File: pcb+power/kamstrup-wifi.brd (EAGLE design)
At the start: 36 x 81.3 mm, 26 parts, among them T1 BT137, T2 BT137, U1 ESP8266-07, U2 MCP1316T-29LE/OT

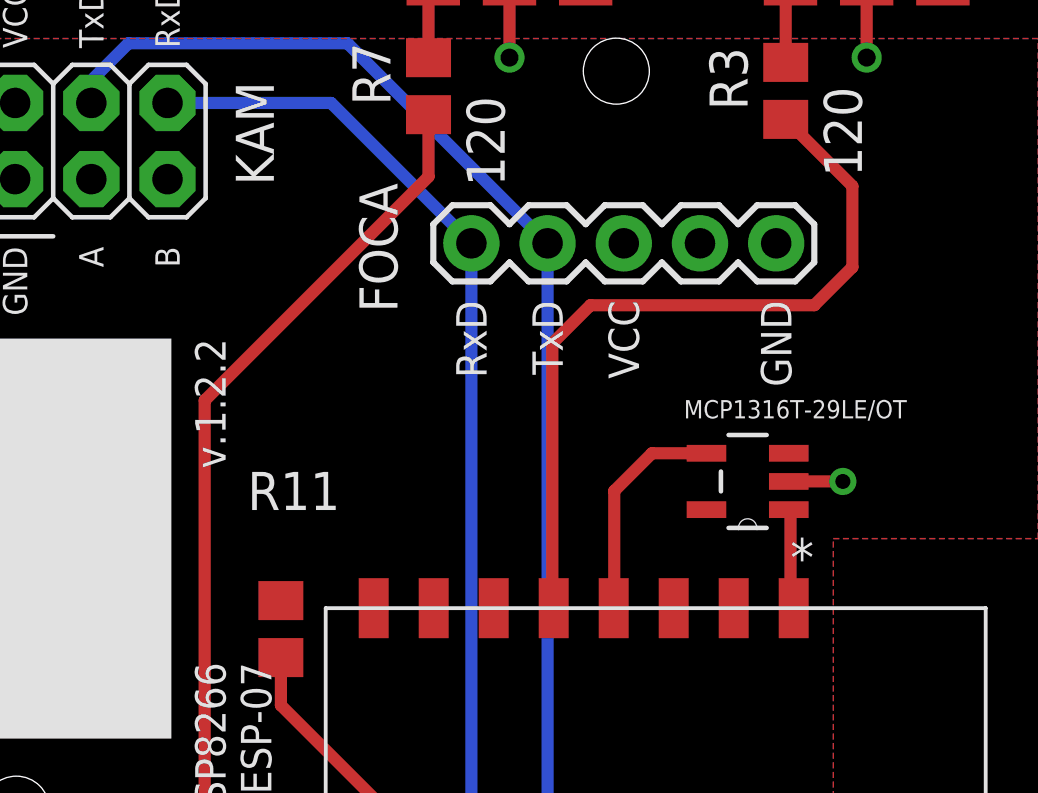
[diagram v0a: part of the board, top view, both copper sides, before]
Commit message: added missing pull down (R12) on pcb
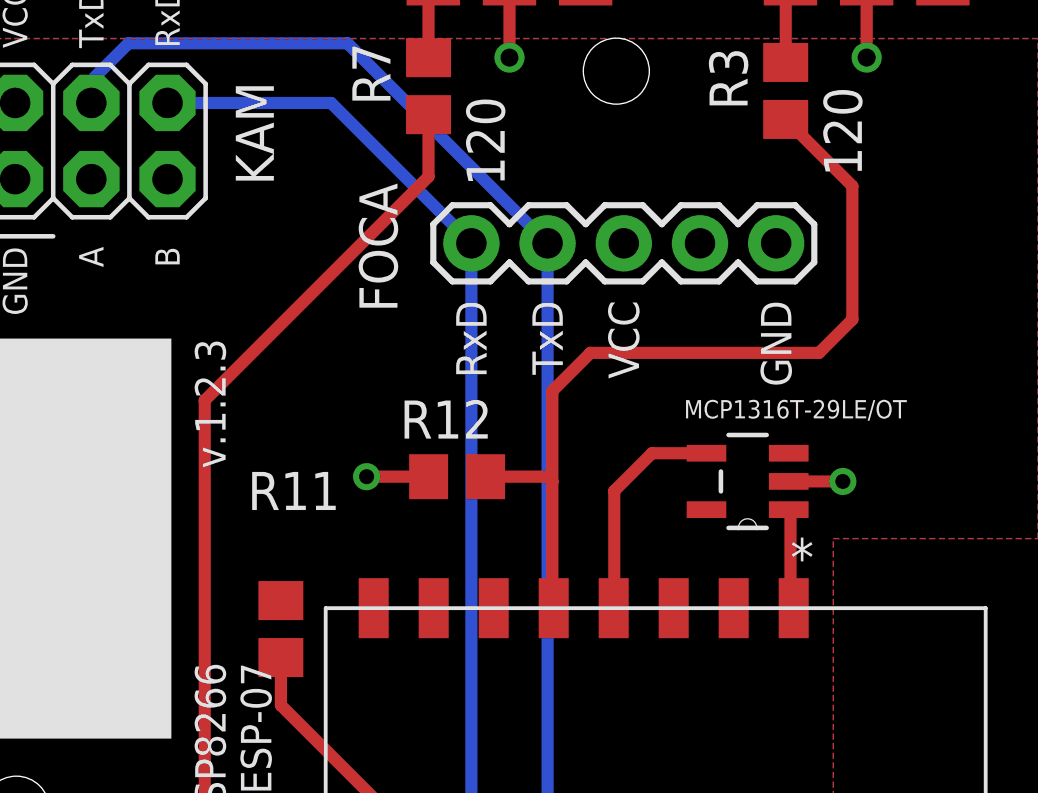
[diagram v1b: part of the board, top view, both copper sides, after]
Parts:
- added R12: 10k, rcl:R0805
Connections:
- net GND: now also R12.1
- net N$11: now also R12.2
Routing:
- net N$11: track 25.7 -> 28.1 mm
- net GND: track 17.8 -> 19.8 mm, vias 4 -> 5
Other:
- board text added: "Part RS# C1, C2 766-1150 JP1, JP2, JP3 821-8701 KAM 702-2937 OK1, OK2 691-2319 R1, R2, R11, R12 721-7820 R3, R7 721-6867 R4, R5, R8, R9 770-8742 R6, R10 770-8798 T1, T2 792-0709"
- board text added: "v.1.2.3"
- board text removed: "Part RS# C1, C2 766-1150 JP1, JP2, JP3 821-8701 KAM 702-2937 OK1, OK2 691-2319 R1, R2, R11 721-7820 R3, R7 721-6867 R4, R5, R8, R9 770-8742 R6, R10 770-8798 T1, T2 792-0709"
- board text removed: "v.1.2.2"

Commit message: reverted pcb to v 1.2.1 2377baf1af9bc101ab4e1265beb616f56084d54c no pull down needed
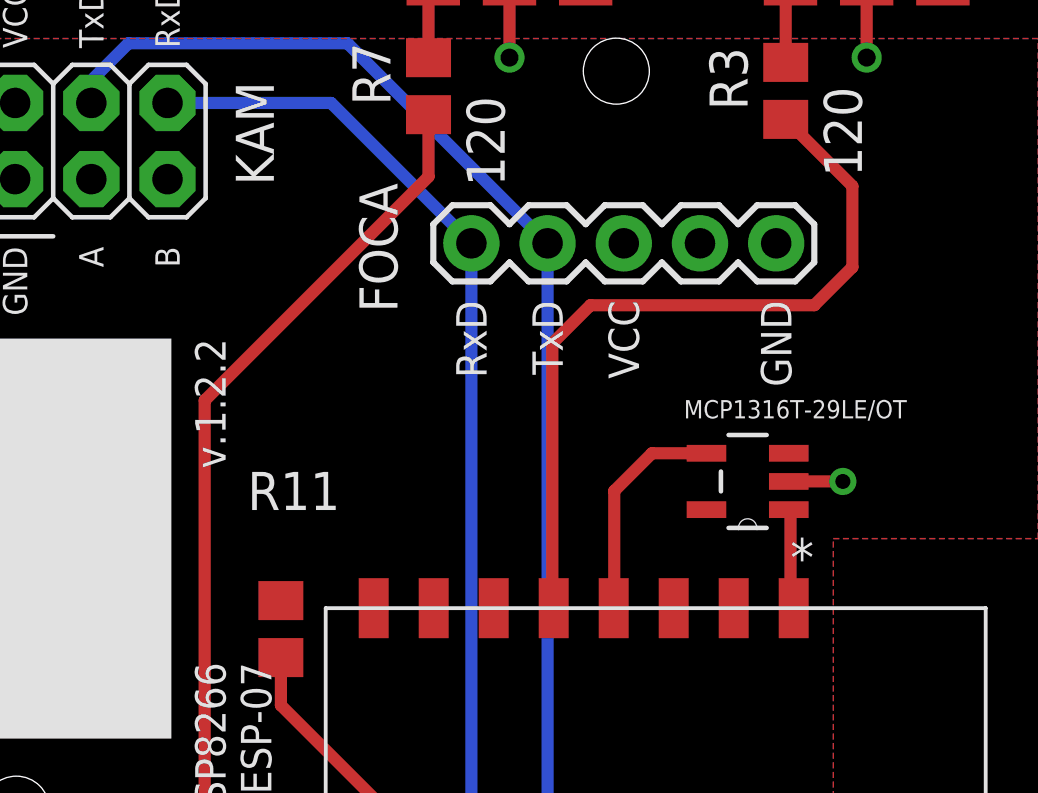
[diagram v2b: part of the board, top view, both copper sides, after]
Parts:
- removed R12: 10k, rcl:R0805
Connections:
- net GND: no longer R12.1
- net N$11: no longer R12.2
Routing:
- net N$11: track 28.1 -> 25.7 mm
- net GND: track 19.8 -> 17.8 mm, vias 5 -> 4
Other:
- board text added: "Part RS# C1, C2 766-1150 JP1, JP2, JP3 821-8701 KAM 702-2937 OK1, OK2 691-2319 R1, R2, R11 721-7820 R3, R7 721-6867 R4, R5, R8, R9 770-8742 R6, R10 770-8798 T1, T2 792-0709"
- board text added: "v.1.2.2"
- board text removed: "Part RS# C1, C2 766-1150 JP1, JP2, JP3 821-8701 KAM 702-2937 OK1, OK2 691-2319 R1, R2, R11, R12 721-7820 R3, R7 721-6867 R4, R5, R8, R9 770-8742 R6, R10 770-8798 T1, T2 792-0709"
- board text removed: "v.1.2.3"
